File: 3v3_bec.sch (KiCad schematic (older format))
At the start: 11 parts

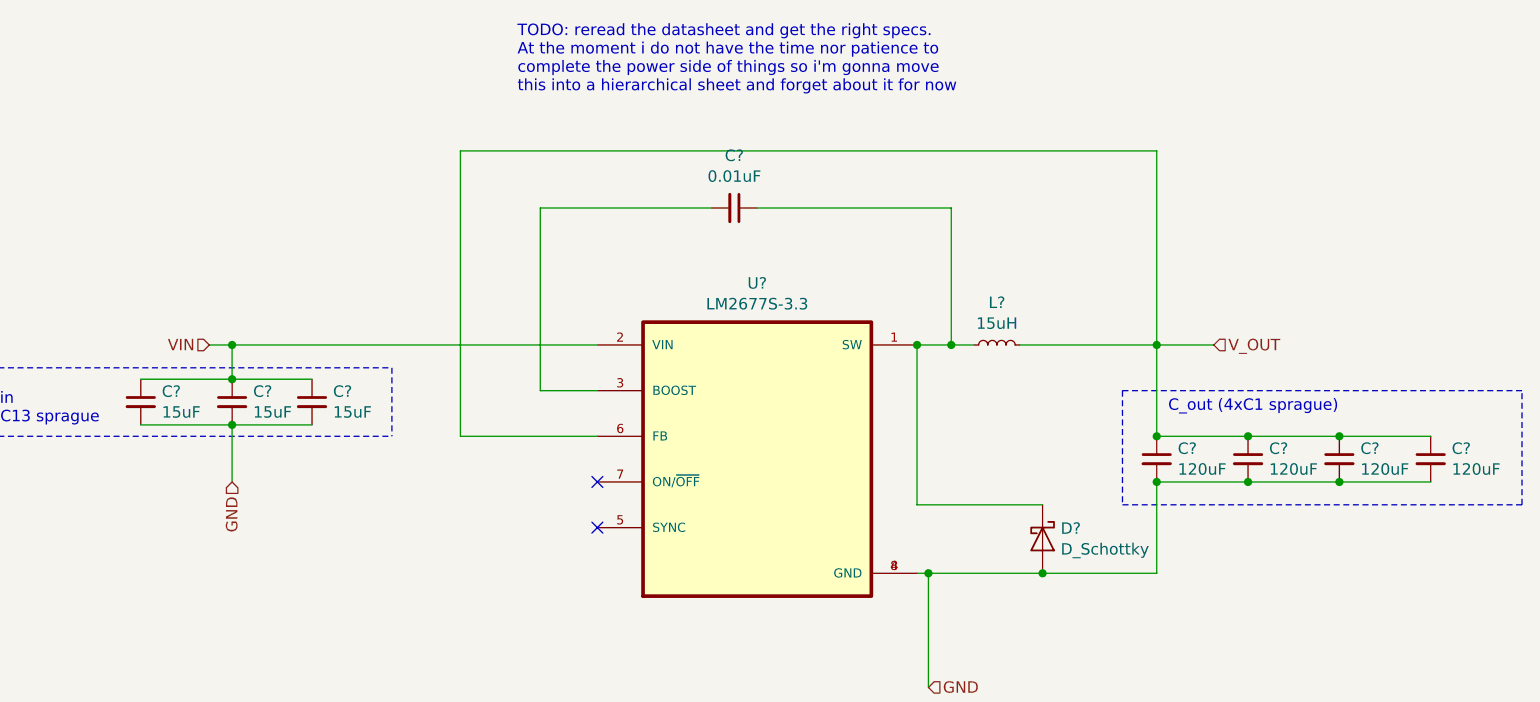
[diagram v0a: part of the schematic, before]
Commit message: update reference ids, assign value to c8
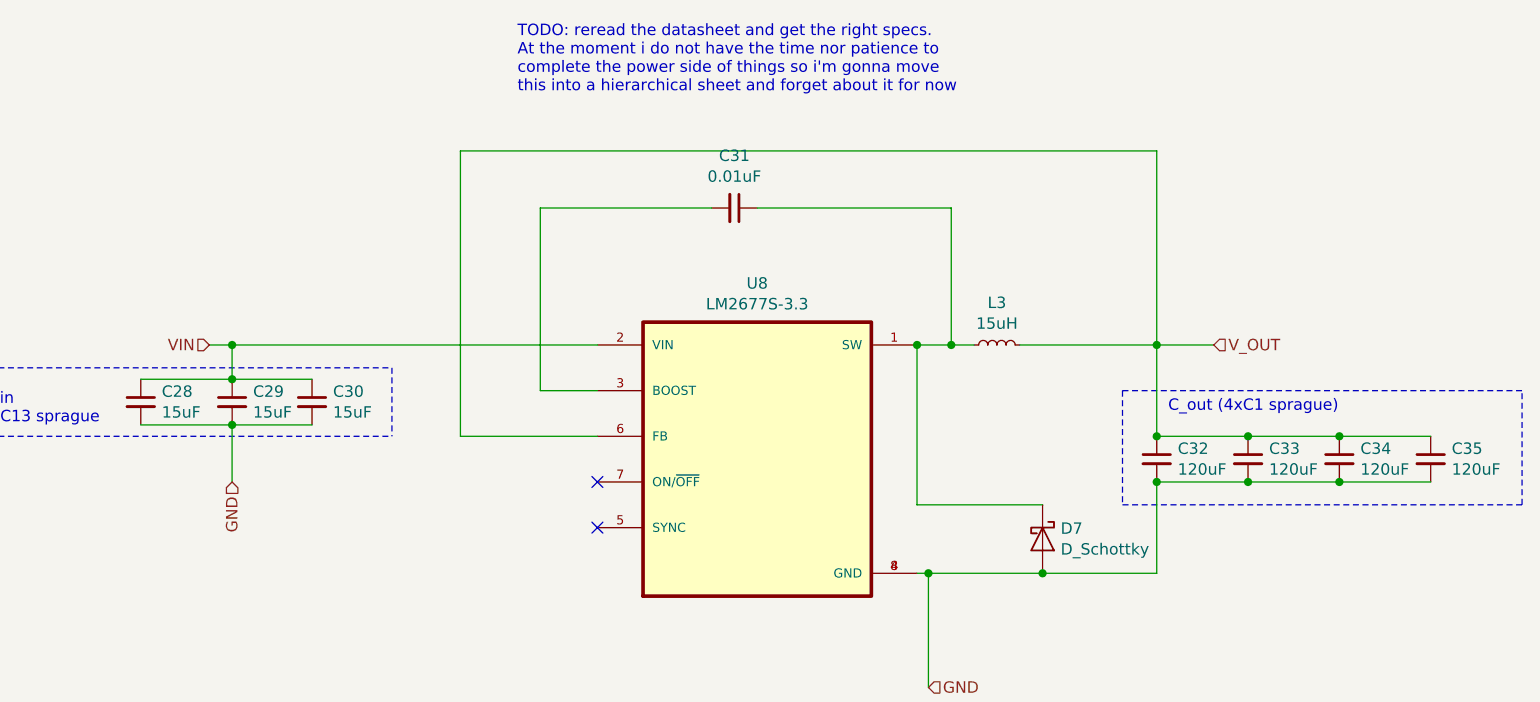
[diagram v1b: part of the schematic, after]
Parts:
- removed C?: 0.01uF, symbol Device:C_Small
- removed D?: D_Schottky, symbol Device:D_Schottky
- removed L?: 15uH, symbol Device:L_Small
- added C31: 0.01uF, symbol Device:C_Small
- added D7: D_Schottky, symbol Device:D_Schottky
- added L3: 15uH, symbol Device:L_Small
- gave numbers to parts that had none: 8
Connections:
- net GND: now also D7.2 (A)
- net V_OUT: now also L3.2
- net at U8.1 (SW): now also C31.1, D7.1 (K), L3.1
- net at U8.3 (BOOST): now also C31.2
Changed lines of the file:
@@
 $Comp
 L Device:D_Schottky D?
-U 1 1 617603E2
+U 1 1 61A7758E
 P 7250 4600
-AR Path="/6175047F/617603E2" Ref="D?"  Part="1"
-AR Path="/617748F9/617603E2" Ref="D?"  Part="1"
-AR Path="/619B79F1/617603E2" Ref="D?"  Part="1"
-AR Path="/619C4F1E/617603E2" Ref="D?"  Part="1"
-AR Path="/619C86ED/617603E2" Ref="D?"  Part="1"
-F 0 "D?" V 7204 4679 50  0000 L CNN
+AR Path="/6175047F/61A7758E" Ref="D?"  Part="1"
+AR Path="/617748F9/61A7758E" Ref="D?"  Part="1"
+AR Path="/619B79F1/61A7758E" Ref="D?"  Part="1"
+AR Path="/619C4F1E/61A7758E" Ref="D?"  Part="1"
+AR Path="/619C86ED/61A7758E" Ref="D7"  Part="1"
+F 0 "D7" V 7204 4679 50  0000 L CNN
 F 1 "D_Schottky" V 7295 4679 50  0000 L CNN
 F 2 "" H 7250 4600 50  0001 C CNN
@@
 $Comp
 L Device:L_Small L?
-U 1 1 61768ED3
+U 1 1 61A7758F
 P 7050 3750
-AR Path="/6175047F/61768ED3" Ref="L?"  Part="1"
-AR Path="/617748F9/61768ED3" Ref="L?"  Part="1"
-AR Path="/619B79F1/61768ED3" Ref="L?"  Part="1"
-AR Path="/619C4F1E/61768ED3" Ref="L?"  Part="1"
-AR Path="/619C86ED/61768ED3" Ref="L?"  Part="1"
-F 0 "L?" V 7235 3750 50  0000 C CNN
+AR Path="/6175047F/61A7758F" Ref="L?"  Part="1"
+AR Path="/617748F9/61A7758F" Ref="L?"  Part="1"
+AR Path="/619B79F1/61A7758F" Ref="L?"  Part="1"
+AR Path="/619C4F1E/61A7758F" Ref="L?"  Part="1"
+AR Path="/619C86ED/61A7758F" Ref="L3"  Part="1"
+F 0 "L3" V 7235 3750 50  0000 C CNN
 F 1 "15uH" V 7144 3750 50  0000 C CNN
 F 2 "" H 7050 3750 50  0001 C CNN
@@
 $Comp
 L Device:C_Small C?
-U 1 1 6176CADF
+U 1 1 61A77590
 P 5900 3150
-AR Path="/6175047F/6176CADF" Ref="C?"  Part="1"
-AR Path="/617748F9/6176CADF" Ref="C?"  Part="1"
-AR Path="/619B79F1/6176CADF" Ref="C?"  Part="1"
-AR Path="/619C4F1E/6176CADF" Ref="C?"  Part="1"
-AR Path="/619C86ED/6176CADF" Ref="C?"  Part="1"
-F 0 "C?" V 5671 3150 50  0000 C CNN
+AR Path="/6175047F/61A77590" Ref="C?"  Part="1"
+AR Path="/617748F9/61A77590" Ref="C?"  Part="1"
+AR Path="/619B79F1/61A77590" Ref="C?"  Part="1"
+AR Path="/619C4F1E/61A77590" Ref="C?"  Part="1"
+AR Path="/619C86ED/61A77590" Ref="C31"  Part="1"
+F 0 "C31" V 5671 3150 50  0000 C CNN
 F 1 "0.01uF" V 5762 3150 50  0000 C CNN
 F 2 "" H 5900 3150 50  0001 C CNN
@@
 TODO: reread the datasheet and get the right specs.\nAt the moment i do not have the time nor patience to \ncomplete the power side of things so i'm gonna move\nthis into a hierarchical sheet and forget about it for now
 $Comp
-L LM2677S-3v3:LM2677S-3.3 U?
+L LM2677S-3v3:LM2677S-3.3 U8
 U 1 1 619CA55E
 P 6000 4250
-F 0 "U?" H 6000 5020 50  0000 C CNN
+F 0 "U8" H 6000 5020 50  0000 C CNN
 F 1 "LM2677S-3.3" H 6000 4929 50  0000 C CNN
 F 2 "TO127P1435X464-8N" H 6000 4250 50  0001 L BNN
@@
 Inductors (L46, 15uH, 5.6A max)\n - Pulse Engineering P0846\n - Coilcraft DO5022P-153HC\n\nC_out:\n - 4xC1(avx tps), 4xC1 (sprague), 4xC3 (kemet)\n\nC_in:\n - 3xC13 (sprague), 4xC12(kemet)\n\nDiode: \n - 6TQ045S\n\n\n\n
 $Comp
-L Device:C_Small C?
+L Device:C_Small C28
 U 1 1 61A18B84
 P 3300 4000
-F 0 "C?" H 3392 4046 50  0000 L CNN
+F 0 "C28" H 3392 4046 50  0000 L CNN
 F 1 "15uF" H 3392 3955 50  0000 L CNN
 F 2 "" H 3300 4000 50  0001 C CNN
@@
 $EndComp
 $Comp
-L Device:C_Small C?
+L Device:C_Small C29
 U 1 1 61A1D43E
 P 3700 4000
-F 0 "C?" H 3792 4046 50  0000 L CNN
+F 0 "C29" H 3792 4046 50  0000 L CNN
 F 1 "15uF" H 3792 3955 50  0000 L CNN
 F 2 "" H 3700 4000 50  0001 C CNN
@@
 $EndComp
 $Comp
-L Device:C_Small C?
+L Device:C_Small C30
 U 1 1 61A1DB55
 P 4050 4000
-F 0 "C?" H 4142 4046 50  0000 L CNN
+F 0 "C30" H 4142 4046 50  0000 L CNN
 F 1 "15uF" H 4142 3955 50  0000 L CNN
 F 2 "" H 4050 4000 50  0001 C CNN
@@
 	2550 4150 2550 3850
 $Comp
-L Device:C_Small C?
+L Device:C_Small C32
 U 1 1 61A276BA
 P 7750 4250
-F 0 "C?" H 7842 4296 50  0000 L CNN
+F 0 "C32" H 7842 4296 50  0000 L CNN
 F 1 "120uF" H 7842 4205 50  0000 L CNN
 F 2 "" H 7750 4250 50  0001 C CNN
@@
 $EndComp
 $Comp
-L Device:C_Small C?
+L Device:C_Small C33
 U 1 1 61A286F2
 P 8150 4250
-F 0 "C?" H 8242 4296 50  0000 L CNN
+F 0 "C33" H 8242 4296 50  0000 L CNN
 F 1 "120uF" H 8242 4205 50  0000 L CNN
 F 2 "" H 8150 4250 50  0001 C CNN
@@
 $EndComp
 $Comp
-L Device:C_Small C?
+L Device:C_Small C34
 U 1 1 61A28EA1
 P 8550 4250
-F 0 "C?" H 8642 4296 50  0000 L CNN
+F 0 "C34" H 8642 4296 50  0000 L CNN
 F 1 "120uF" H 8642 4205 50  0000 L CNN
 F 2 "" H 8550 4250 50  0001 C CNN
@@
 $EndComp
 $Comp
-L Device:C_Small C?
+L Device:C_Small C35
 U 1 1 61A2984E
 P 8950 4250
-F 0 "C?" H 9042 4296 50  0000 L CNN
+F 0 "C35" H 9042 4296 50  0000 L CNN
 F 1 "120uF" H 9042 4205 50  0000 L CNN
 F 2 "" H 8950 4250 50  0001 C CNN

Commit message: no longer a hat lol
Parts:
- C28, C29, C30, C32, C33, C34, C35: footprint (none) -> Capacitor_Tantalum_SMD:CP_EIA-7260-38_AVX-R_Pad2.68x6.30mm_HandSolder
- C31: footprint (none) -> Capacitor_SMD:C_0805_2012Metric_Pad1.15x1.40mm_HandSolder
- D7: footprint (none) -> TO254P1521X483-4N:TO254P1521X483-4N
- L3: footprint (none) -> DR127-150-R:INDM125125X800N
- U8: footprint TO127P1435X464-8N -> LM2677S-3v3:TO127P1435X464-8N
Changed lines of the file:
@@
 F 0 "D7" V 7204 4679 50  0000 L CNN
 F 1 "D_Schottky" V 7295 4679 50  0000 L CNN
-F 2 "" H 7250 4600 50  0001 C CNN
+F 2 "TO254P1521X483-4N:TO254P1521X483-4N" H 7250 4600 50  0001 C CNN
 F 3 "~" H 7250 4600 50  0001 C CNN
 	1    7250 4600
@@
 F 0 "L3" V 7235 3750 50  0000 C CNN
 F 1 "15uH" V 7144 3750 50  0000 C CNN
-F 2 "" H 7050 3750 50  0001 C CNN
+F 2 "DR127-150-R:INDM125125X800N" H 7050 3750 50  0001 C CNN
 F 3 "~" H 7050 3750 50  0001 C CNN
 	1    7050 3750
@@
 F 0 "C31" V 5671 3150 50  0000 C CNN
 F 1 "0.01uF" V 5762 3150 50  0000 C CNN
-F 2 "" H 5900 3150 50  0001 C CNN
+F 2 "Capacitor_SMD:C_0805_2012Metric_Pad1.15x1.40mm_HandSolder" H 5900 3150 50  0001 C CNN
 F 3 "~" H 5900 3150 50  0001 C CNN
 	1    5900 3150
@@
 F 0 "U8" H 6000 5020 50  0000 C CNN
 F 1 "LM2677S-3.3" H 6000 4929 50  0000 C CNN
-F 2 "TO127P1435X464-8N" H 6000 4250 50  0001 L BNN
+F 2 "LM2677S-3v3:TO127P1435X464-8N" H 6000 4250 50  0001 L BNN
 F 3 "" H 6000 4250 50  0001 L BNN
 	1    6000 4250
@@
 F 0 "C28" H 3392 4046 50  0000 L CNN
 F 1 "15uF" H 3392 3955 50  0000 L CNN
-F 2 "" H 3300 4000 50  0001 C CNN
+F 2 "Capacitor_Tantalum_SMD:CP_EIA-7260-38_AVX-R_Pad2.68x6.30mm_HandSolder" H 3300 4000 50  0001 C CNN
 F 3 "~" H 3300 4000 50  0001 C CNN
 	1    3300 4000
@@
 F 0 "C29" H 3792 4046 50  0000 L CNN
 F 1 "15uF" H 3792 3955 50  0000 L CNN
-F 2 "" H 3700 4000 50  0001 C CNN
+F 2 "Capacitor_Tantalum_SMD:CP_EIA-7260-38_AVX-R_Pad2.68x6.30mm_HandSolder" H 3700 4000 50  0001 C CNN
 F 3 "~" H 3700 4000 50  0001 C CNN
 	1    3700 4000
@@
 F 0 "C30" H 4142 4046 50  0000 L CNN
 F 1 "15uF" H 4142 3955 50  0000 L CNN
-F 2 "" H 4050 4000 50  0001 C CNN
+F 2 "Capacitor_Tantalum_SMD:CP_EIA-7260-38_AVX-R_Pad2.68x6.30mm_HandSolder" H 4050 4000 50  0001 C CNN
 F 3 "~" H 4050 4000 50  0001 C CNN
 	1    4050 4000
@@
 F 0 "C32" H 7842 4296 50  0000 L CNN
 F 1 "120uF" H 7842 4205 50  0000 L CNN
-F 2 "" H 7750 4250 50  0001 C CNN
+F 2 "Capacitor_Tantalum_SMD:CP_EIA-7260-38_AVX-R_Pad2.68x6.30mm_HandSolder" H 7750 4250 50  0001 C CNN
 F 3 "~" H 7750 4250 50  0001 C CNN
 	1    7750 4250
@@
 F 0 "C33" H 8242 4296 50  0000 L CNN
 F 1 "120uF" H 8242 4205 50  0000 L CNN
-F 2 "" H 8150 4250 50  0001 C CNN
+F 2 "Capacitor_Tantalum_SMD:CP_EIA-7260-38_AVX-R_Pad2.68x6.30mm_HandSolder" H 8150 4250 50  0001 C CNN
 F 3 "~" H 8150 4250 50  0001 C CNN
 	1    8150 4250
@@
 F 0 "C34" H 8642 4296 50  0000 L CNN
 F 1 "120uF" H 8642 4205 50  0000 L CNN
-F 2 "" H 8550 4250 50  0001 C CNN
+F 2 "Capacitor_Tantalum_SMD:CP_EIA-7260-38_AVX-R_Pad2.68x6.30mm_HandSolder" H 8550 4250 50  0001 C CNN
 F 3 "~" H 8550 4250 50  0001 C CNN
 	1    8550 4250
@@
 F 0 "C35" H 9042 4296 50  0000 L CNN
 F 1 "120uF" H 9042 4205 50  0000 L CNN
-F 2 "" H 8950 4250 50  0001 C CNN
+F 2 "Capacitor_Tantalum_SMD:CP_EIA-7260-38_AVX-R_Pad2.68x6.30mm_HandSolder" H 8950 4250 50  0001 C CNN
 F 3 "~" H 8950 4250 50  0001 C CNN
 	1    8950 4250
